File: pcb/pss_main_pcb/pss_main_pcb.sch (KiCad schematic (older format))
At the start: 64 parts

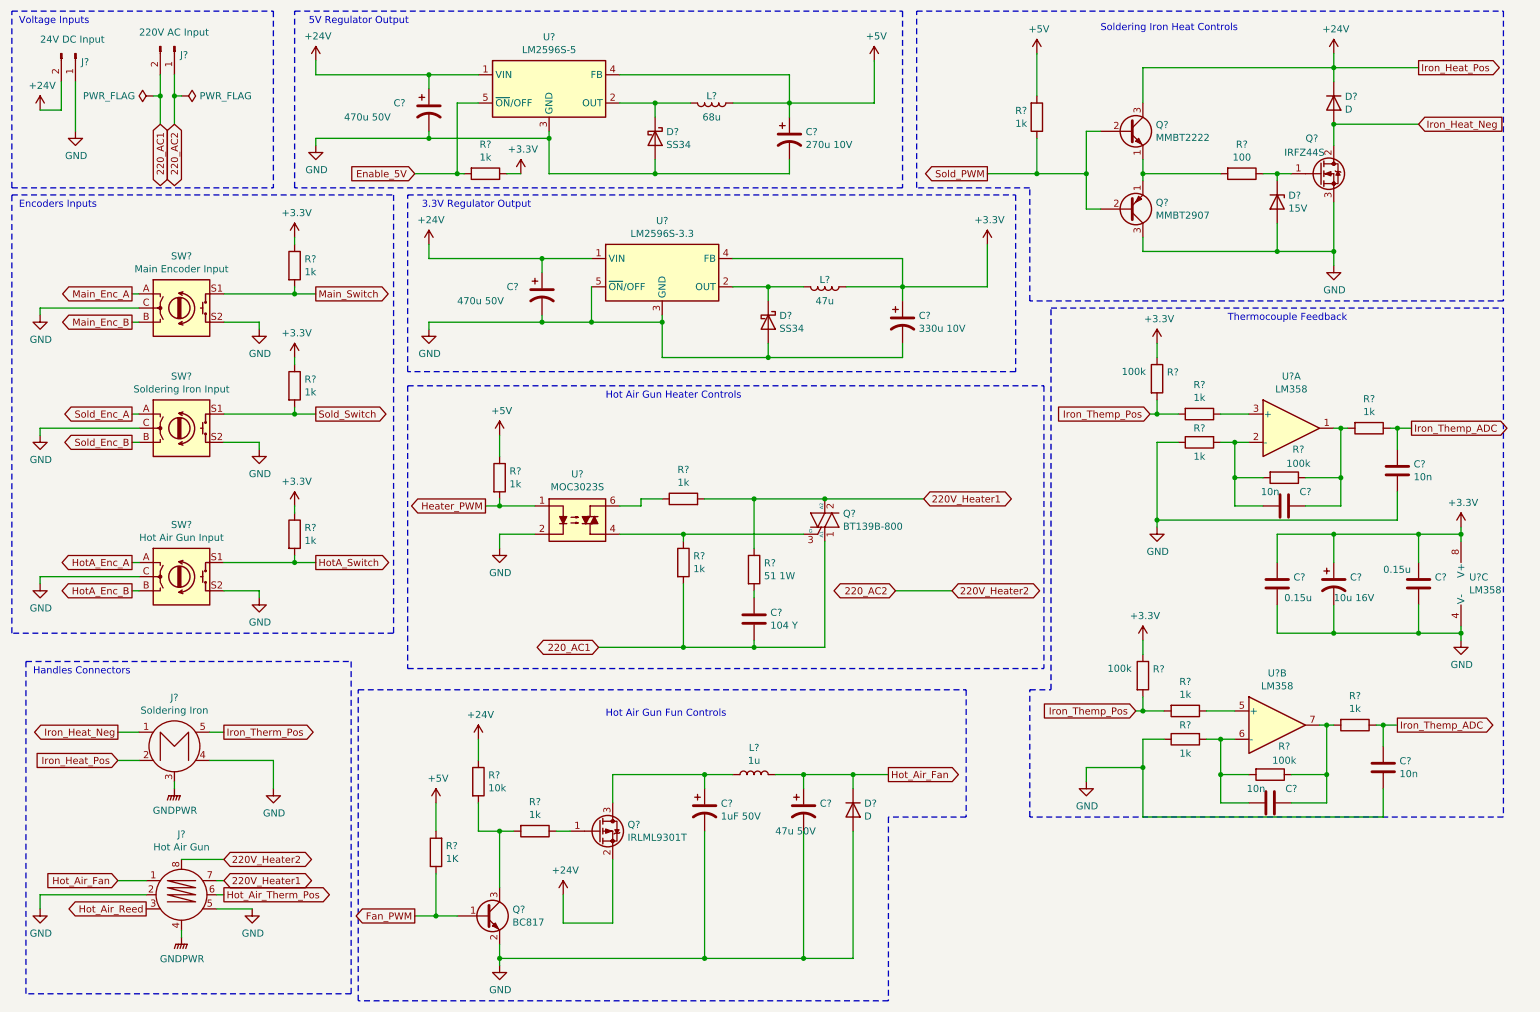
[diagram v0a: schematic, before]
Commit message: Add hierarchy lists
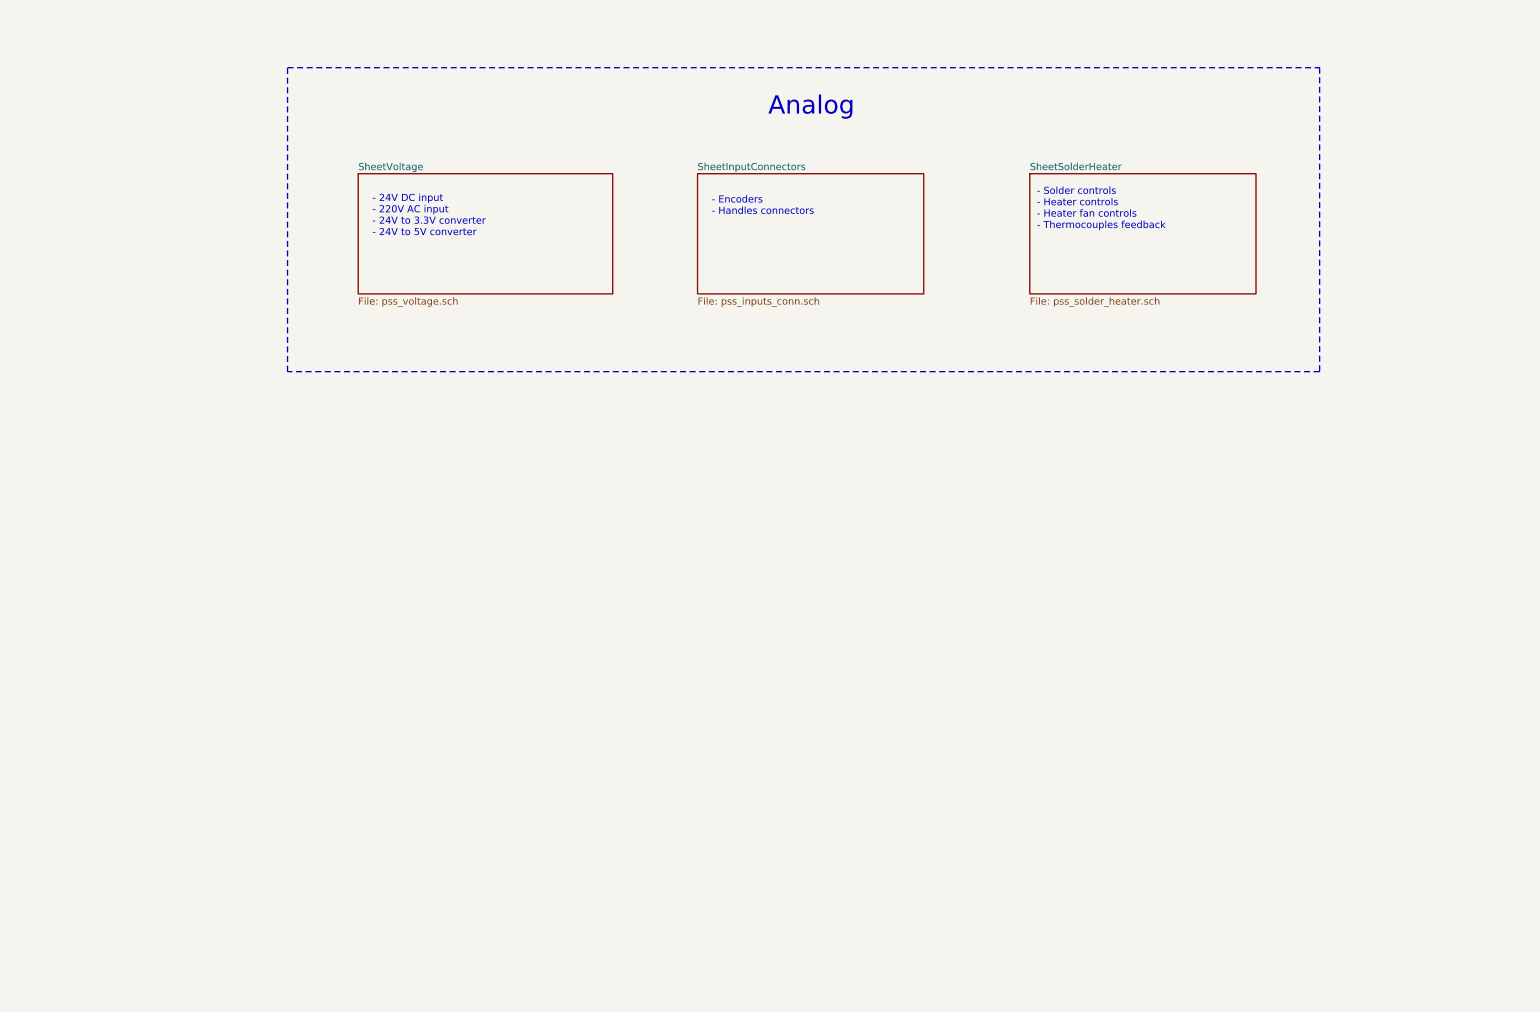
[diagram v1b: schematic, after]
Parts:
- removed C?: 104 Y, symbol Device:C
- removed C? (x2): 470u 50V, symbol Device:CP1
- removed C?: 270u 10V, symbol Device:CP1
- removed C?: 330u 10V, symbol Device:CP1
- removed C?: 47u 50V, symbol Device:CP1
- removed C?: 1uF 50V, symbol Device:CP1
- removed C? (x2): 0.15u, symbol Device:C
- removed C? (x4): 10n, symbol Device:C
- removed C?: 10u 16V, symbol Device:CP1
- removed D? (x2): D, symbol Device:D
- removed D?: 15V, symbol Device:D_Zener
- removed D? (x2): SS34, symbol Device:D_Schottky
- removed J?: 220V AC Input, symbol Connector:Conn_01x02_Male
- removed J?: 24V DC Input, symbol Connector:Conn_01x02_Male
- removed J?: Soldering Iron, symbol gx16_conn:GX16-M5_connector
- removed J?: Hot Air Gun, symbol gx16_conn:GX16-M8_connector
- removed L?: 68u, symbol Device:L
- removed L?: 47u, symbol Device:L
- removed L?: 1u, symbol Device:L
- removed Q?: BT139B-800, Package_TO_SOT_THT:SOT-404, symbol Triac_custom:BT139B-800
- removed Q?: IRLML9301T, Package_TO_SOT_SMD:SOT-23, symbol Transistors_custom:IRLML9301T
- removed Q?: IRFZ44S, Package_TO_SOT_THT:TO-220-3_Vertical, symbol Transistors_custom:IRFZ44S
- removed Q?: BC817, Package_TO_SOT_SMD:SOT-23, symbol Transistor_BJT:BC817
- removed Q?: MMBT2222, Package_TO_SOT_THT:TO-92_Inline, symbol Transistors_custom:MMBT2222
- removed Q?: MMBT2907, Package_TO_SOT_THT:TO-92_Inline, symbol Transistors_custom:MMBT2907
- removed R? (x15): 1k, symbol Device:R
- removed R?: 100, symbol Device:R
- removed R?: 51 1W, symbol Device:R
- removed R?: 10k, symbol Device:R
- removed R?: 1K, symbol Device:R
- removed R? (x4): 100k, symbol Device:R
- removed SW?: Main Encoder Input, symbol Device:Rotary_Encoder_Switch
- removed SW?: Soldering Iron Input, symbol Device:Rotary_Encoder_Switch
- removed SW?: Hot Air Gun Input, symbol Device:Rotary_Encoder_Switch
- removed U?: MOC3023S, symbol Opto_custom:MOC3023S
- removed U?: LM2596S-5, Package_TO_SOT_SMD:TO-263-5_TabPin3, symbol Regulator_Switching:LM2596S-5
- removed U?: LM2596S-3.3, Package_TO_SOT_SMD:TO-263-5_TabPin3, symbol Regulator_Switching:LM2596S-3.3
- removed U? (x3): LM358, symbol Amplifier_Operational:LM358
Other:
- note added: "- 24V DC input\n- 220V AC input \n- 24V to 3.3V converter\n- 24V to 5V converter"
- note added: "- Encoders\n- Handles connectors"
- note added: "- Solder controls\n- Heater controls\n- Heater fan controls\n- Thermocouples feedback\n"
- note added: "Analog"
- note removed: "3.3V Regulator Output"
- note removed: "5V Regulator Output"
- note removed: "Encoders Inputs"
- note removed: "Handles Connectors\n"
- note removed: "Hot Air Gun Fun Controls\n"
- note removed: "Hot Air Gun Heater Controls\n"
- note removed: "Soldering Iron Heat Controls\n"
- note removed: "Thermocouple Feedback\n"
- note removed: "Voltage Inputs"
